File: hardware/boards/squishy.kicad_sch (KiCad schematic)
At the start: 46 parts, among them J1 USB_B_Micro, J2 Conn_02x26_Top_Bottom, J3 Conn_02x05_Odd_Even, J4 Conn_01x04, Q1 Q_PMOS_DGS, U1 W25N01GVZEIG, U2 ICE40HX8K-BG121, U3 USB3318, X1 48MHz, X2 16MHz

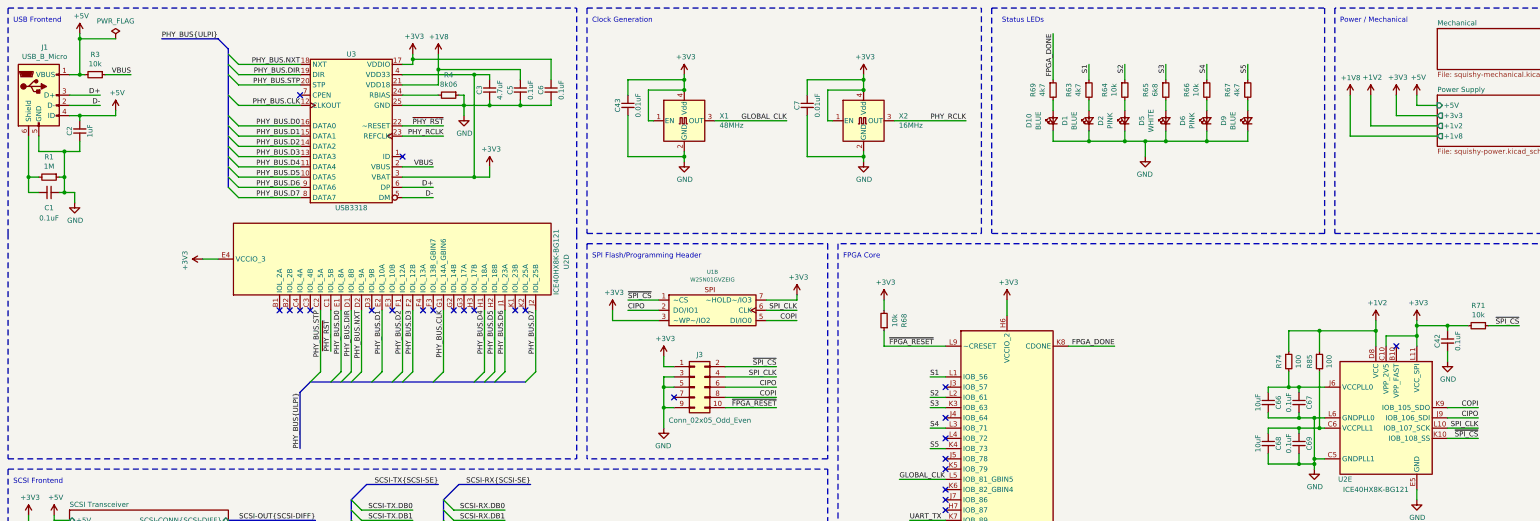
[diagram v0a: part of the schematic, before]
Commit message: hardware: Gutted the ULPI interface in favor of directly driving the USB diff pair due to gateware timing issues
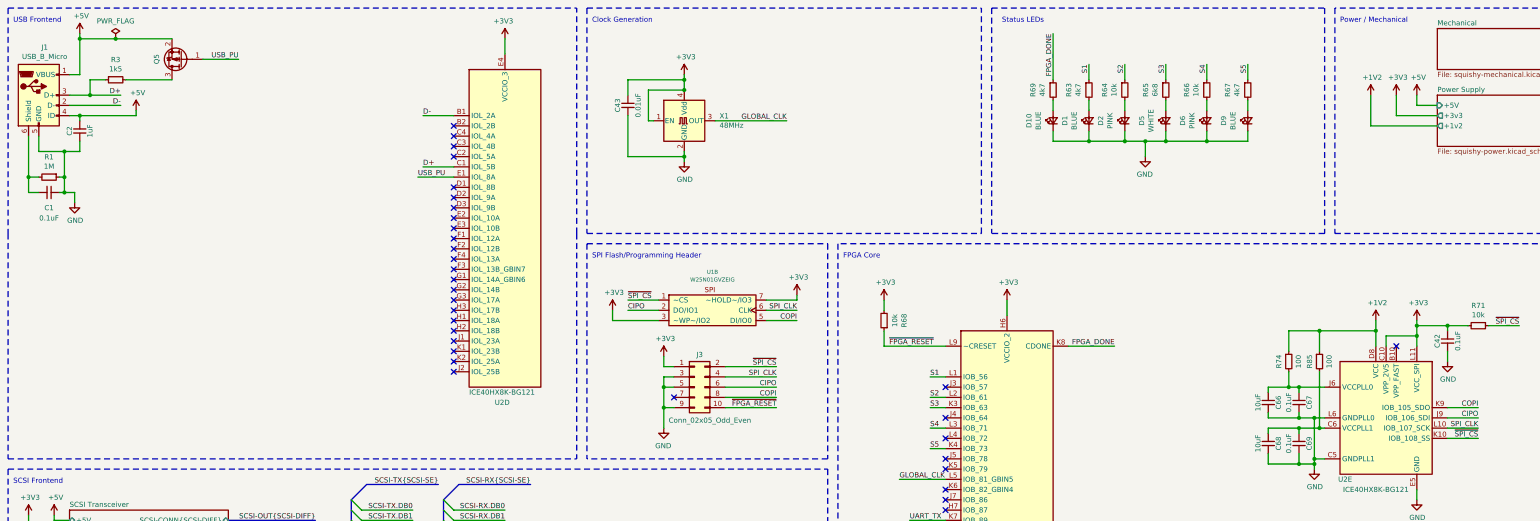
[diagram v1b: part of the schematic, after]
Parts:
- removed C3: 4.7uF, Capacitor_SMD:C_0603_1608Metric, symbol Device:C_Small
- removed C5, C6: 0.1uF, Capacitor_SMD:C_0603_1608Metric, symbol Device:C_Small
- removed C7: 0.01uF, Capacitor_SMD:C_0603_1608Metric, symbol Device:C_Small
- removed R4: 8k06, Resistor_SMD:R_0603_1608Metric, symbol Device:R_Small
- removed U3: USB3318, Package_DFN_QFN:QFN-24-1EP_4x4mm_P0.5mm_EP2.6x2.6mm, symbol lethalbit:USB3318
- removed X2: 16MHz, Oscillator:Oscillator_SMD_Abracon_ASE-4Pin_3.2x2.5mm, symbol Oscillator:ASE-xxxMHz
- added Q5: Q_PMOS_DGS, Package_TO_SOT_SMD:SOT-323_SC-70, symbol Device:Q_PMOS_GSD
- R3: value 10k -> 1k5; MFR Vishay Dale -> (none); MPN CRCW060310K0FKEA -> (none)
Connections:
- net VBUS is gone; now on net D+: R3.1
- net ~{PHY_RST} is gone; now on net D+: U2.C1 (IOL_5B)
- net +5V: now also Q5.2 (S); no longer R3.2
- net D-: now also U2.B1 (IOL_2A)
- net PHY_BUS.CLK: no longer names the net of U2.G1 (IOL_14A_GBIN6)
- net PHY_BUS.D0 renamed USB_PU
- net USB_PU: now also Q5.1 (G)
- net PHY_BUS.D1: no longer names the net of U2.E2 (IOL_10A)
- net PHY_BUS.D2: no longer names the net of U2.F1 (IOL_12A)
- net PHY_BUS.D3: no longer names the net of U2.F2 (IOL_12B)
- net PHY_BUS.D4: no longer names the net of U2.H1 (IOL_18A)
- net PHY_BUS.D5: no longer names the net of U2.H2 (IOL_18B)
- net PHY_BUS.D6: no longer names the net of U2.J1 (IOL_23A)
- net PHY_BUS.D7: no longer names the net of U2.J2 (IOL_25B)
- net PHY_BUS.DIR: no longer names the net of U2.D1 (IOL_8B)
- net PHY_BUS.NXT: no longer names the net of U2.D2 (IOL_9A)
- net PHY_BUS.STP: no longer names the net of U2.C2 (IOL_5A)
- new net: Q5.3 (D), R3.2
- no-connect marks 30 -> 38
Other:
- sheet Power Supply ports: added none; removed +1v8
- moved on the sheet: U2D
